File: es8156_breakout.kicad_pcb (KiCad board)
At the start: 2 copper layers, 24.4 x 31.5 mm, 9 parts, among them J1 Headphones, J2 Conn_01x12, J3 Conn_01x03, U1 ES8156

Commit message: silkscreen adjustments
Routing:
- net VP: track 25.9 -> 26.7 mm
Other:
- board text added: "v0.1 tresonic 6/25"
- board text removed: "C1-4: 1u"
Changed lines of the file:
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@@
 		(at 39.095 42.754 90)
 		(property "Reference" "U1"
-			(at 1.524 3.302 180)
+			(at 2.794 1.778 180)
 			(layer "F.SilkS")
 			(effects
@@
 		)
 		(property "Value" "ES8156"
-			(at 0 5.08 180)
+			(at 3.048 1.27 180)
 			(layer "F.Fab")
 			(effects
@@
 		(tags "Through hole pin header THT 1x03 2.54mm single row")
 		(property "Reference" "J3"
-			(at 0 -2.38 0)
+			(at -2.794 -1.016 0)
 			(layer "F.SilkS")
 			(effects
@@
 		)
 	)
-	(gr_text "C1-4: 1u"
-		(at 33.507 52.66 0)
-		(layer "F.SilkS")
-		(effects
-			(font
-				(size 1 1)
-				(thickness 0.2)
-				(bold yes)
-			)
-			(justify left)
-		)
-	)
 	(gr_text "VA"
 		(at 27.665 32.34 0)
@@
 		)
 	)
+	(gr_text "v0.1 tresonic 6/25"
+		(at 46.969 53.676 0)
+		(layer "F.SilkS")
+		(effects
+			(font
+				(size 1 1)
+				(thickness 0.1)
+			)
+			(justify right bottom)
+		)
+	)
 	(gr_text "VD"
 		(at 27.665 27.26 0)
@@
 	(segment
 		(start 32.364 37.039)
+		(end 25.125 29.8)
+		(width 0.2)
+		(layer "F.Cu")
+		(net 4)
+	)
+	(segment
+		(start 36.682 38.182)
 		(end 35.539 37.039)
-		(width 0.2)
-		(layer "F.Cu")
-		(net 4)
-	)
-	(segment
-		(start 35.539 37.039)
-		(end 37.952 39.452)
 		(width 0.2)
 		(layer "F.Cu")
@@
 	)
 	(segment
+		(start 37.952 38.182)
+		(end 36.682 38.182)
+		(width 0.2)
+		(layer "F.Cu")
+		(net 4)
+	)
+	(segment
 		(start 39.895 44.254)
 		(end 39.895 44.316)
@@
 	)
 	(segment
-		(start 25.125 29.8)
+		(start 35.539 37.039)
 		(end 32.364 37.039)
 		(width 0.2)
@@
 	)
 	(via
-		(at 37.952 39.452)
+		(at 37.952 38.182)
 		(size 0.6)
 		(drill 0.3)
@@
 		(width 0.2)
 		(layer "B.Cu")
+		(net 4)
+	)
+	(segment
+		(start 37.952 38.182)
+		(end 37.952 39.452)
+		(width 0.2)
+		(layer "B.Cu")

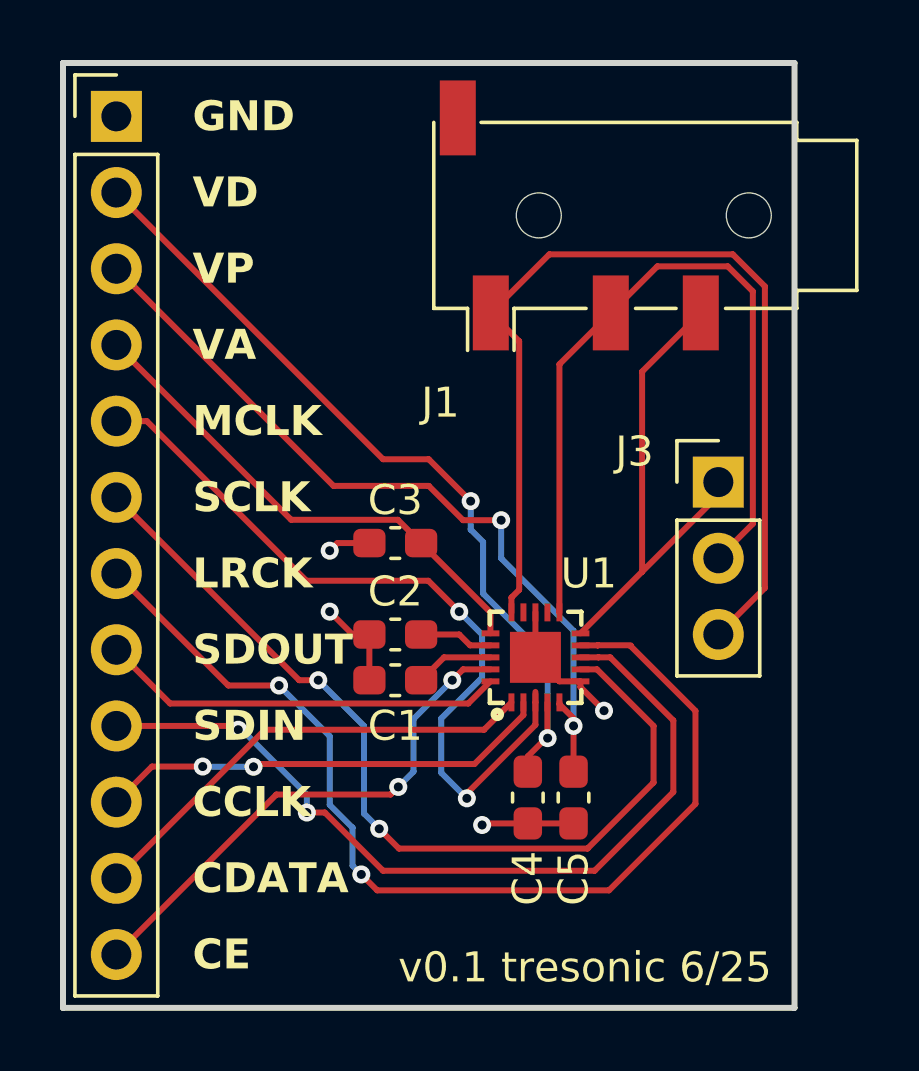
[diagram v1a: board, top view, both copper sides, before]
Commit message: use lcsc imported audio jack
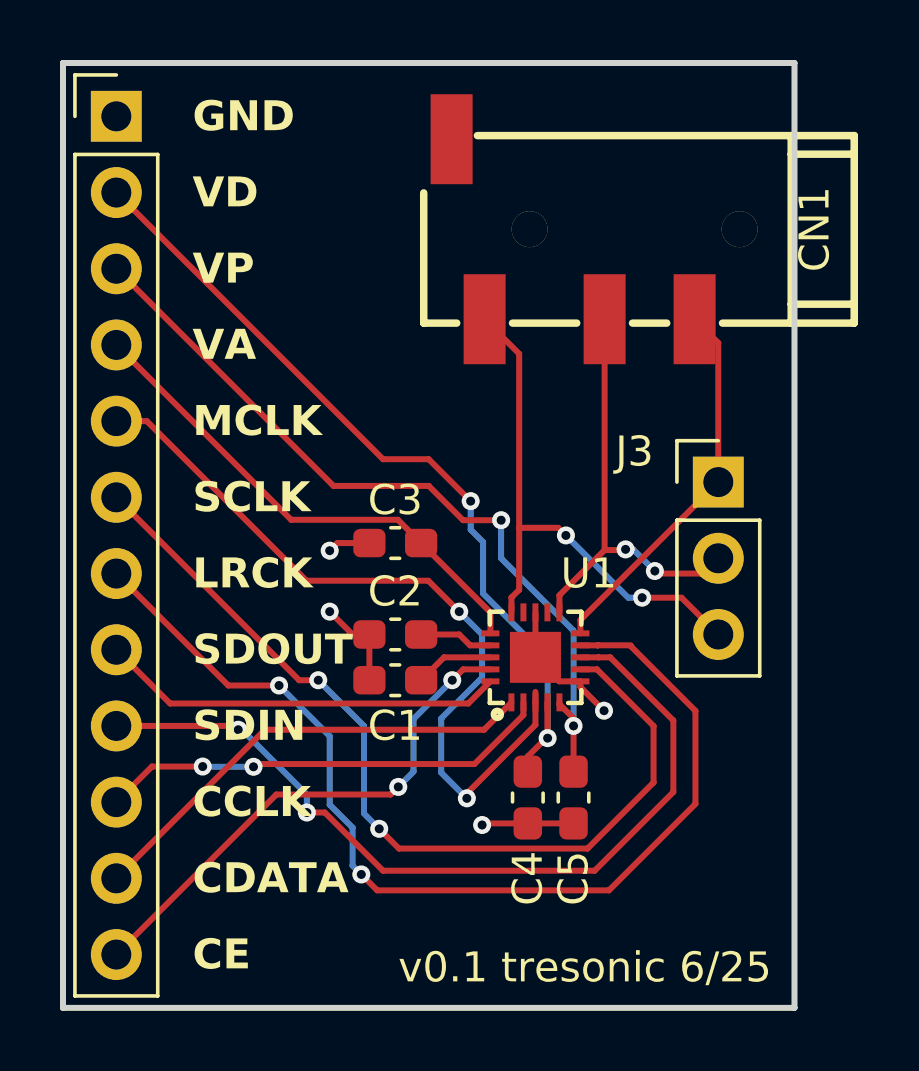
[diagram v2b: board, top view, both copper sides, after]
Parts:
- removed J1: Headphones, Connector_Audio:Jack_3.5mm_PJ320D_Horizontal
- added CN1: PJ-320D, lcsc:AUDIO-SMD_PJ-320D, F.Cu at (40.4, 28.5)
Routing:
- net /Left: track 33.1 -> 18.5 mm, vias 0 -> 2
- net /Right: track 25.8 -> 14.7 mm, vias 0 -> 2
- net /HPCOM: track 16.4 -> 12.7 mm
